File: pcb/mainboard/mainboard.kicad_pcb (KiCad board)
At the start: 2 copper layers, 87.6 x 63.1 mm, 56 parts, among them J1 V_IN, J3 Control Board, J4 M1, J5 M2, J7 TIP, K1 SANYOU_SRD_Form_C, Q1 NMOS, Q2 NMOS, U2 TPS54331DDA, U3 TMC2208_SILENTSTEPSTICK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

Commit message: Update PCB Change Buck Converter Vout  from 3.3V to 5V
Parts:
- removed R6: 0, Resistor_SMD:R_0603_1608Metric_Pad0.98x0.95mm_HandSolder
- added R1: 10k, Resistor_SMD:R_0603_1608Metric_Pad0.98x0.95mm_HandSolder, F.Cu at (154.5, 74.8)
- added R2: 1k, Resistor_SMD:R_0603_1608Metric_Pad0.98x0.95mm_HandSolder, F.Cu at (154.5, 73.2)
- D3: value D -> 1N4148-0603
- R12, R13, R16: value R -> 1k
- R14: value R -> 5k
- R7: value 10.2k -> 10k
- R8: value 3.24k -> 1k
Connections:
- net /BUCK_3V3_BOOT renamed /BUCK_5V_BOOT
- net /BUCK_3V3_COMP renamed /BUCK_5V_COMP
- net /BUCK_3V3_EN renamed /BUCK_5V_EN
- net /BUCK_3V3_PH renamed /BUCK_5V_PH
- net /BUCK_3V3_SS renamed /BUCK_5V_SS
- C19 pad 1: +3.3V -> +5V
- C20 pad 1: +3.3V -> +5V
- C23 pad 1: +3.3V -> +5V
- C24 pad 1: +3.3V -> +5V
- C25 pad 1: +3.3V -> +5V
- D3 pad 1: +3.3V -> +5V
- J3 pad 2: OLED_3V3 -> +3.3V
- K1 pad 4: +3.3V -> +5V
- K1 pad 5: +3.3V -> +5V
- L1 pad 2: +3.3V -> +5V
- R10 pad 1: +3.3V -> +5V
- R12 pad 1: +3.3V -> +5V
- R13 pad 1: +3.3V -> +5V
- R7 pad 2: Net-(R6-Pad1) -> +5V
- R8 pad 2: VSENSE -> Net-(R1-Pad1)
- R9 pad 1: +3.3V -> +5V
- U3 pad JP2_7: +3.3V -> +5V
- U4 pad JP2_7: +3.3V -> +5V
- U5 pad 5: +3.3V -> +5V
- U6 pad 1: +3.3V -> +5V
- U6 pad 2: +3.3V -> +5V
- U6 pad 25: OLED_3V3 -> +3.3V
- U6 pad 26: OLED_3V3 -> +3.3V
- U6 pad 32: +3.3V -> +5V
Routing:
- net +5V: track 0.00 -> 220.1 mm, vias 0 -> 10
- net +3.3V: track 216.3 -> 10.8 mm, vias 10 -> 0
- net OLED_3V3: track 10.8 -> 0.00 mm
- net Net-(R1-Pad1): track 0.00 -> 4.81 mm
- net VSENSE: track 11.1 -> 15.1 mm
- net Net-(R6-Pad1): track 1.83 -> 0.00 mm
- net GND: track 55.5 -> 55.4 mm, vias 22 -> 21
- added copper zone on B.Cu, net +5V
- added copper zone on F.Cu, net +5V
- removed copper zone on B.Cu, net +3.3V
- removed copper zone on F.Cu, net +3.3V

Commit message: Update PCB | Requested Changes
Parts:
- added JP1: SolderJumper_2_Open, Jumper:SolderJumper-2_P1.3mm_Open_TrianglePad1.0x1.5mm, F.Cu at (145.6, 86.1)
- added JP2: SolderJumper_2_Open, Jumper:SolderJumper-2_P1.3mm_Open_TrianglePad1.0x1.5mm, F.Cu at (140.0, 86.1)
- added JP3: SolderJumper_2_Open, Jumper:SolderJumper-2_P1.3mm_Open_TrianglePad1.0x1.5mm, F.Cu at (170.7, 84.2)
- moved R11 0.69 mm to (174.9, 79.1)
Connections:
- C19 pad 1: +5V -> /BUCK_5V_OUT
- C20 pad 1: +5V -> /BUCK_5V_OUT
- C25 pad 1: +5V -> /INA_VIN
- L1 pad 2: +5V -> /BUCK_5V_OUT
- R10 pad 1: +5V -> /INA_VIN
- R12 pad 1: +5V -> /BUCK_5V_OUT
- R7 pad 2: +5V -> /BUCK_5V_OUT
- R9 pad 1: +5V -> /INA_VIN
- U5 pad 5: +5V -> /INA_VIN
- U6 pad 1: +5V -> /uC_VCC
- U6 pad 2: +5V -> /uC_VCC
- U6 pad 32: +5V -> /uC_VCC
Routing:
- net /uC_VCC: track 0.00 -> 65.9 mm
- net +5V: track 220.1 -> 160.1 mm
- net /INA_VIN: track 0.00 -> 19.2 mm
- net /BUCK_5V_OUT: track 0.00 -> 12.5 mm
- net INA+: track 19.9 -> 22.8 mm
- added copper zone on F.Cu, net /BUCK_5V_OUT
- added copper zone on F.Cu, net /INA_VIN
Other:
- board text added: "5V"
- board text added: "KN NaMi Tip Etcher v1.1 Adam Matysiak Jakub Klimkowski"
- board text removed: "3.3V"
- board text removed: "KN NaMi Tip Etcher v1.0 Adam Matysiak Jakub Klimkowski"

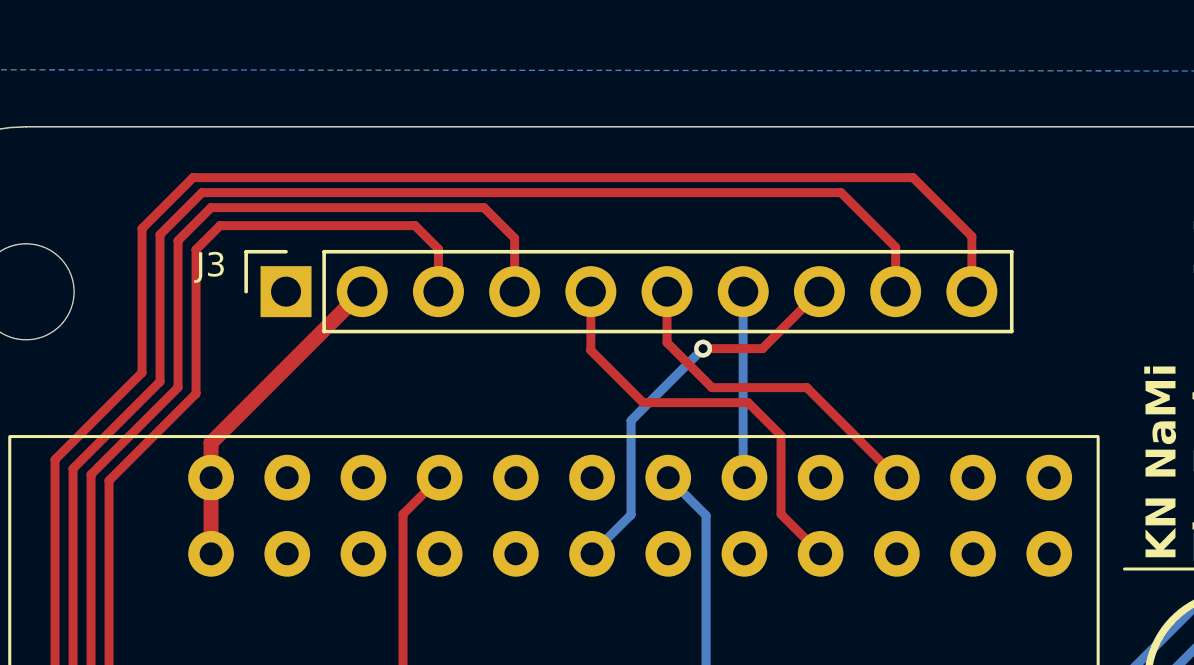
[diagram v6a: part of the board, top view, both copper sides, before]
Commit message: Change OLED Connector Size
Changed size of an OLED connector from 2.54mm to 2.00mm to match its size from other related project.
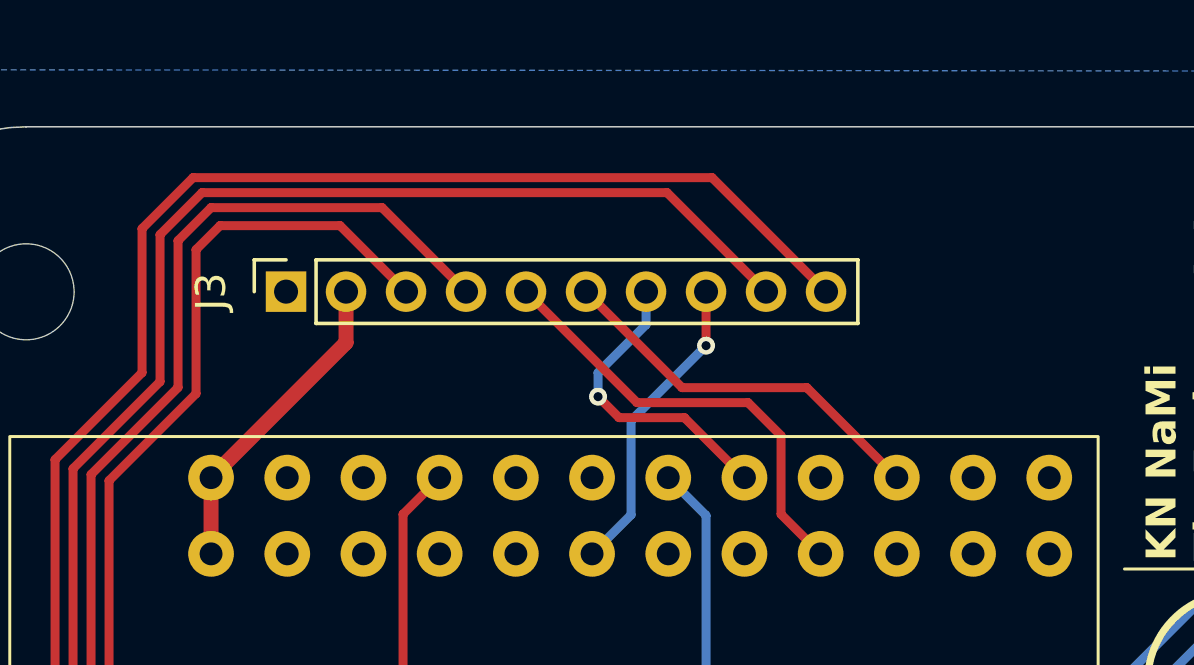
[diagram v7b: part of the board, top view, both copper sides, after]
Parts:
- J3: footprint Connector_PinSocket_2.54mm:PinSocket_1x10_P2.54mm_Vertical -> Connector_PinSocket_2.00mm:PinSocket_1x10_P2.00mm_Vertical
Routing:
- net ENC_SIG_B: track 80.0 -> 74.1 mm
- net ENC_SIG_A: track 71.2 -> 66.0 mm
- net OLED_CS: track 6.22 -> 10.2 mm, vias 0 -> 1
- net ENC_BTN: track 13.0 -> 10.3 mm
- net OLED_SCK: track 51.7 -> 49.0 mm
- net OLED_MOSI: track 50.1 -> 48.2 mm
- net OLED_RESET: track 11.2 -> 12.9 mm
- net OLED_DC: track 14.0 -> 15.0 mm

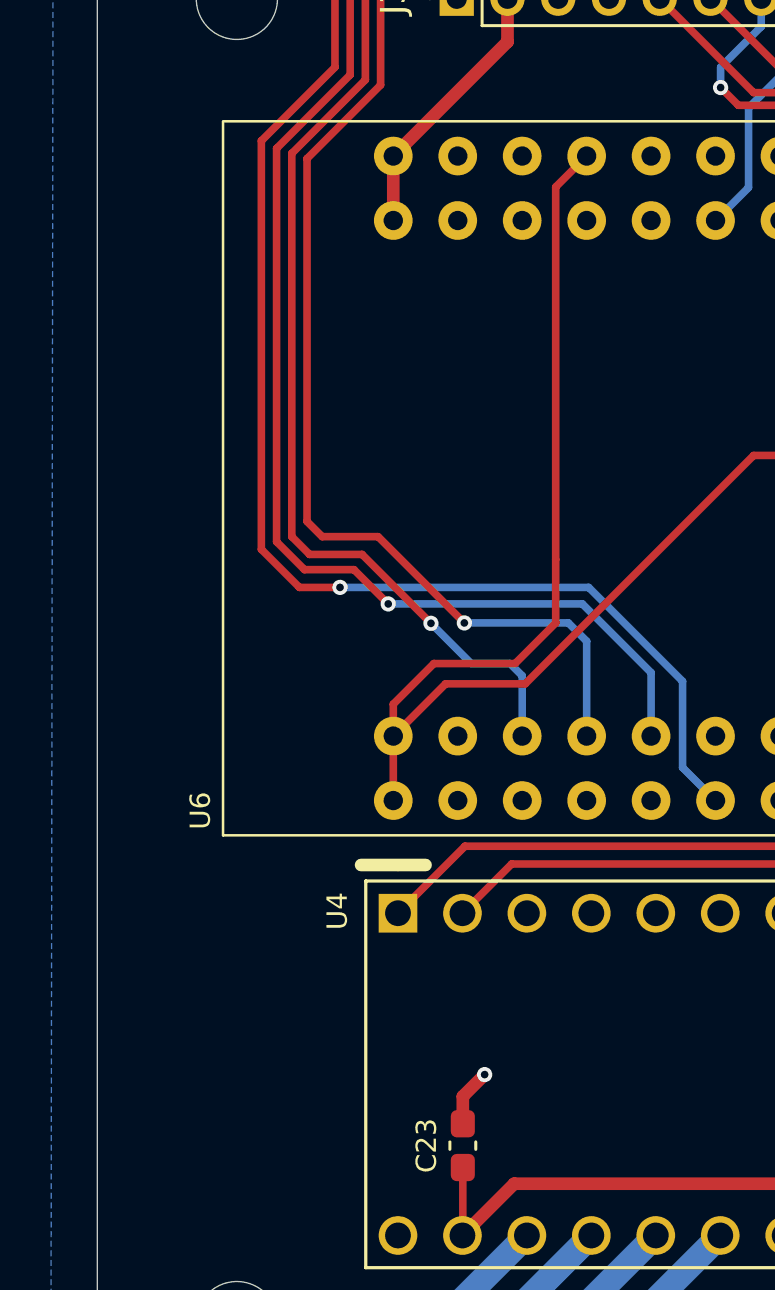
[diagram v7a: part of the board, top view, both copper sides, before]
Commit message: Add Limit Switches
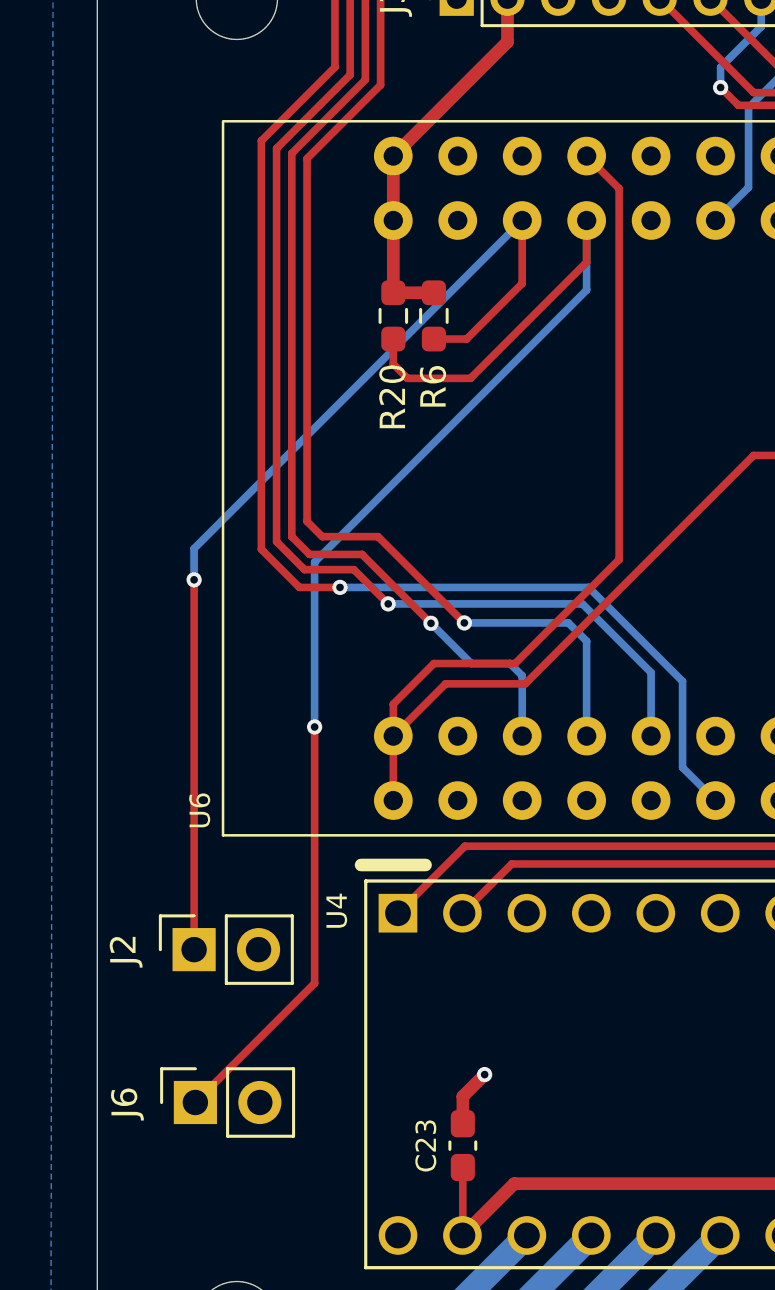
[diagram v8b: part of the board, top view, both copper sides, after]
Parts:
- added J2: Conn_01x02, Connector_PinSocket_2.54mm:PinSocket_1x02_P2.54mm_Vertical, F.Cu at (100.5, 105.6)
- added J6: Conn_01x02, Connector_PinSocket_2.54mm:PinSocket_1x02_P2.54mm_Vertical, F.Cu at (100.6, 111.6)
- added R20: 10k, Resistor_SMD:R_0603_1608Metric_Pad0.98x0.95mm_HandSolder, F.Cu at (108.4, 80.6)
- added R6: 10k, Resistor_SMD:R_0603_1608Metric_Pad0.98x0.95mm_HandSolder, F.Cu at (110.0, 80.6)
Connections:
- U6 pad 29: unconnected-(U6-PB10-Pad29) -> LIMIT_SWITCH_1
- U6 pad 31: unconnected-(U6-PB2-Pad31) -> LIMIT_SWITCH_2
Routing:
- net LIMIT_SWITCH_2: track 0.00 -> 53.5 mm, vias 0 -> 1
- net LIMIT_SWITCH_1: track 0.00 -> 41.0 mm, vias 0 -> 1
- net +3.3V: track 10.6 -> 15.1 mm
- net /uC_VCC: track 65.9 -> 66.9 mm
